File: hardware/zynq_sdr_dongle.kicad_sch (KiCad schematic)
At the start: 13 parts, among them J10 Conn_01x13_Male, J11 Conn_01x16_Male

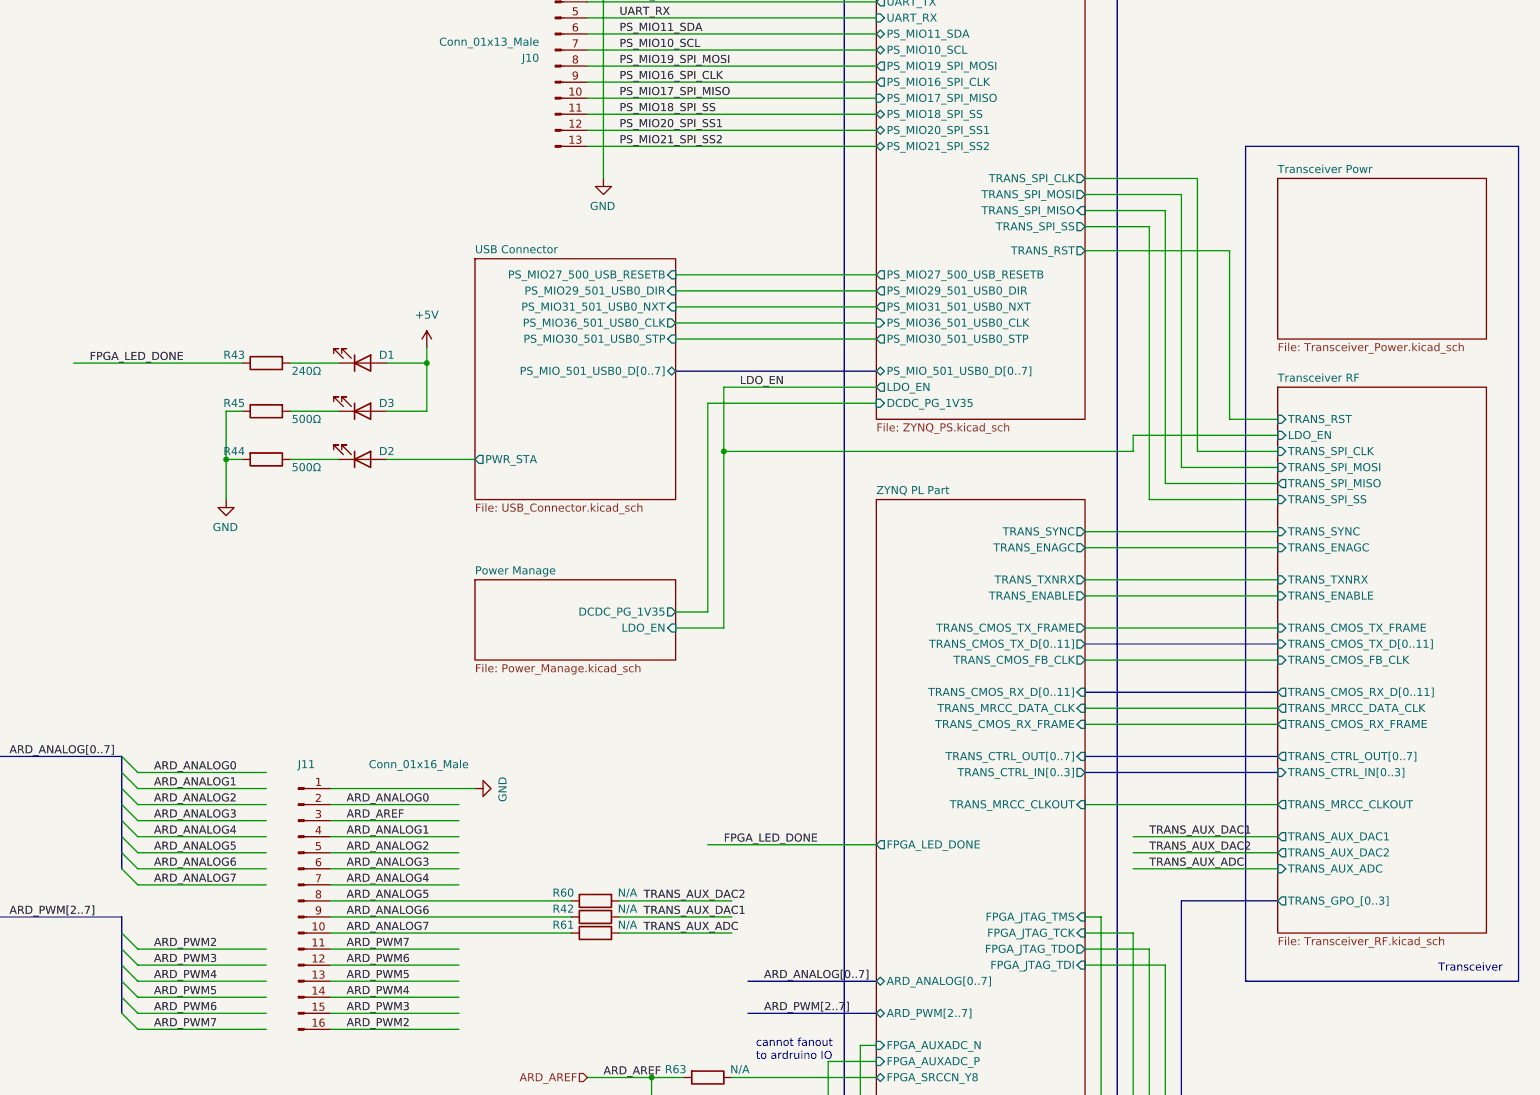
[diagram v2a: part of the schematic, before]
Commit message: Add PS I2C pullup resistor
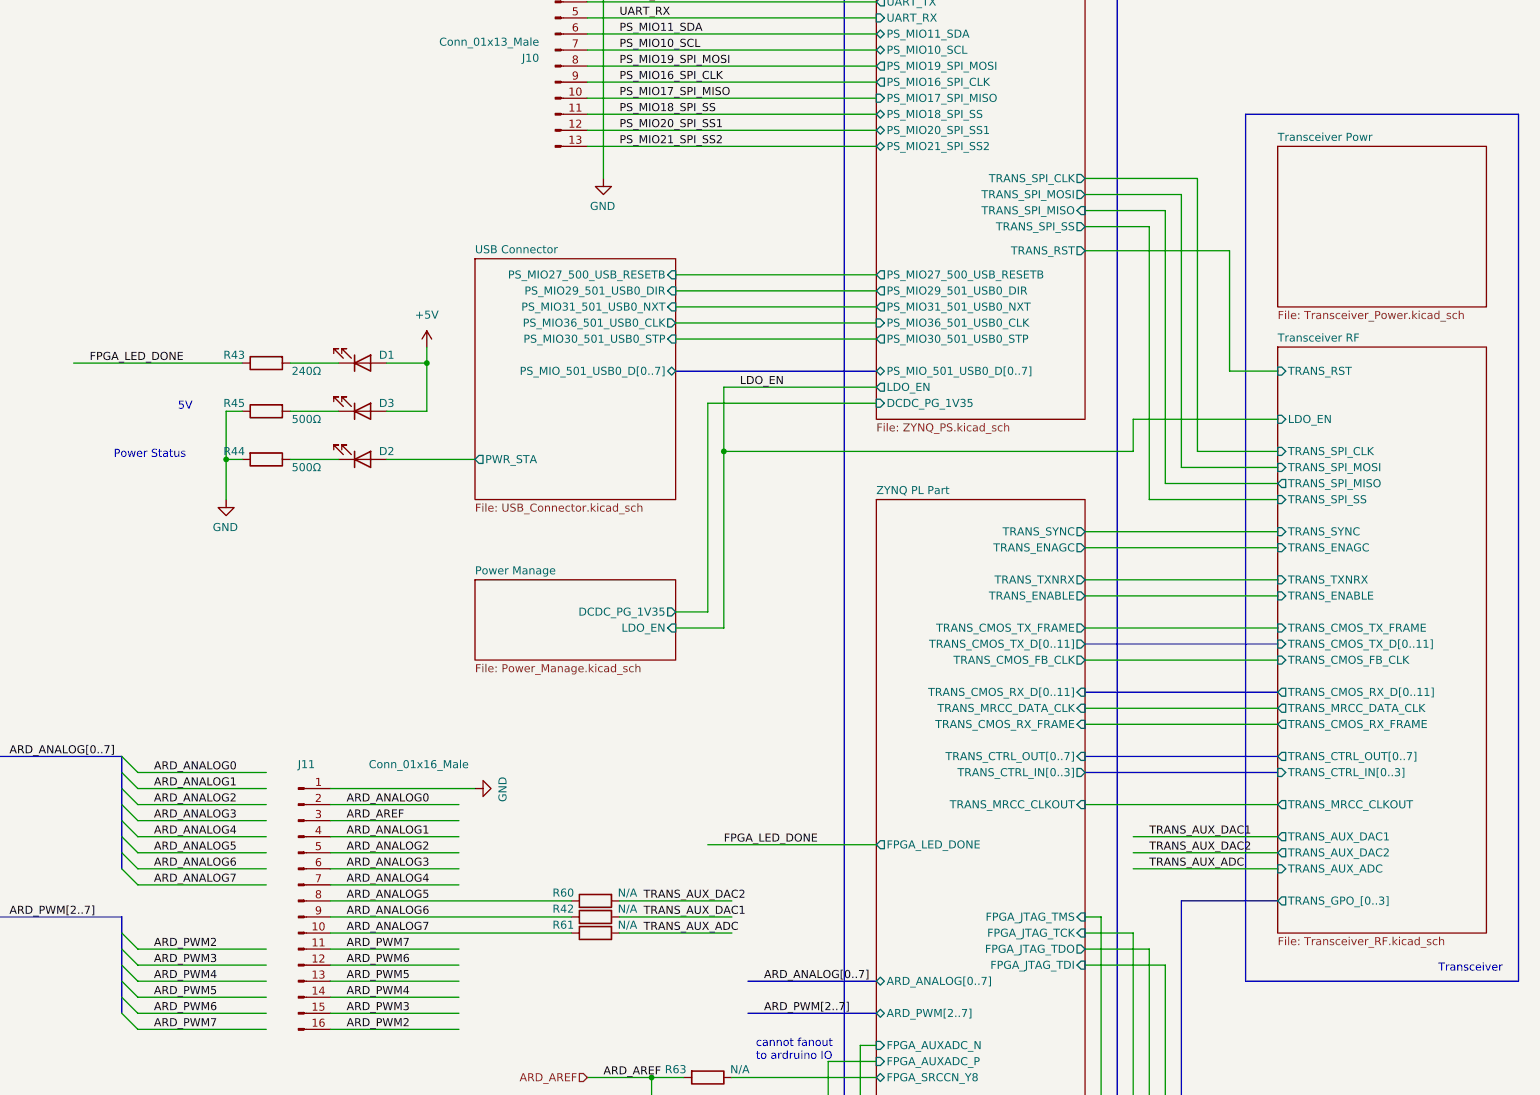
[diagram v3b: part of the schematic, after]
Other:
- note added: "5V"
- note added: "Power Status"
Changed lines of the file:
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@@
     (stroke (width 0) (type default))
   )
-  (wire (pts (xy 259.08 101.6) (xy 251.46 101.6))
+  (wire (pts (xy 259.08 93.98) (xy 251.46 93.98))
     (stroke (width 0) (type default))
   )
@@
     (stroke (width 0) (type default))
   )
-  (wire (pts (xy 236.22 104.14) (xy 259.08 104.14))
+  (wire (pts (xy 236.22 101.6) (xy 259.08 101.6))
     (stroke (width 0) (type default))
   )
@@
     (stroke (width 0) (type default))
   )
-  (wire (pts (xy 251.46 101.6) (xy 251.46 74.93))
+  (wire (pts (xy 251.46 93.98) (xy 251.46 74.93))
     (stroke (width 0) (type default))
   )
@@
     (stroke (width 0) (type default))
   )
-  (wire (pts (xy 236.22 106.68) (xy 236.22 104.14))
+  (wire (pts (xy 236.22 106.68) (xy 236.22 101.6))
     (stroke (width 0) (type default))
   )
@@
     (stroke (width 0) (type default))
   )
-  (rectangle (start 254 58.42) (end 297.18 190.5)
+  (rectangle (start 254 53.34) (end 297.18 190.5)
     (stroke (width 0.1524) (type default))
     (fill (type none))
@@
     (fill (type none))
   )
+  (text "5V" (at 85.09 100.33 0)
+    (effects (font (size 1.27 1.27)) (justify left bottom))
+  )
   (text "Transceiver" (at 284.48 189.23 0)
     (effects (font (size 1.27 1.27)) (justify left bottom))
@@
   )
   (text "cannot fanout\nto ardruino IO\n" (at 176.53 203.2 0)
+    (effects (font (size 1.27 1.27)) (justify left bottom))
+  )
+  (text "Power Status\n" (at 74.93 107.95 0)
     (effects (font (size 1.27 1.27)) (justify left bottom))
   )
@@
     )
   )
-  (sheet (at 259.08 96.52) (size 33.02 86.36) (fields_autoplaced)
+  (sheet (at 259.08 90.17) (size 33.02 92.71) (fields_autoplaced)
     (stroke (width 0.1524) (type solid))
     (fill (color 0 0 0 0.0000))
-    (property "Sheetname" "Transceiver RF" (id 0) (at 259.08 95.8084 0)
+    (property "Sheetname" "Transceiver RF" (id 0) (at 259.08 89.4584 0)
       (effects (font (size 1.27 1.27)) (justify left bottom))
     )
@@
       (effects (font (size 1.27 1.27)) (justify left))
     )
-    (pin "TRANS_RST" input (at 259.08 101.6 180)
-      (effects (font (size 1.27 1.27)) (justify left))
-    )
-    (pin "LDO_EN" input (at 259.08 104.14 180)
-      (effects (font (size 1.27 1.27)) (justify left))
-    )
-  )
-  (sheet (at 259.08 63.5) (size 33.02 25.4) (fields_autoplaced)
+    (pin "TRANS_RST" input (at 259.08 93.98 180)
+      (effects (font (size 1.27 1.27)) (justify left))
+    )
+    (pin "LDO_EN" input (at 259.08 101.6 180)
+      (effects (font (size 1.27 1.27)) (justify left))
+    )
+  )
+  (sheet (at 259.08 58.42) (size 33.02 25.4) (fields_autoplaced)
     (stroke (width 0.1524) (type solid))
     (fill (color 0 0 0 0.0000))
-    (property "Sheetname" "Transceiver Powr" (id 0) (at 259.08 62.7884 0)
+    (property "Sheetname" "Transceiver Powr" (id 0) (at 259.08 57.7084 0)
       (effects (font (size 1.27 1.27)) (justify left bottom))
     )
-    (property "Sheetfile" "Transceiver_Power.kicad_sch" (id 1) (at 259.08 89.4846 0)
+    (property "Sheetfile" "Transceiver_Power.kicad_sch" (id 1) (at 259.08 84.4046 0)
       (effects (font (size 1.27 1.27)) (justify left top))
     )
@@
       (reference "#PWR0237") (unit 1) (value "GND") (footprint "")
     )
-    (path "/2e492126-6191-42ba-8e02-c3a9e141c50a/6311da68-6122-4903-be68-cdff269f6d29"
-      (reference "#PWR0238") (unit 1) (value "GND") (footprint "")
-    )
-    (path "/2e492126-6191-42ba-8e02-c3a9e141c50a/a6f39143-8618-4dc1-9481-e0a08978eabf"
-      (reference "#PWR0239") (unit 1) (value "+1V8") (footprint "")
+    (path "/2e492126-6191-42ba-8e02-c3a9e141c50a/5f5e850e-342f-41c6-81d1-bb27c4f59d7c"
+      (reference "#PWR0238") (unit 1) (value "+1V8") (footprint "")
+    )
+    (path "/2e492126-6191-42ba-8e02-c3a9e141c50a/45708189-6cf6-4828-a1a1-fe879b822edb"
+      (reference "#PWR0239") (unit 1) (value "GND") (footprint "")
     )
     (path "/639f24e7-f472-4c97-971a-e363c3f9fd3c/19b194a1-aaa8-4204-9d7a-386064fa933a"
@@
       (reference "#PWR0260") (unit 1) (value "+1V8") (footprint "")
     )
+    (path "/2e492126-6191-42ba-8e02-c3a9e141c50a/a756a93b-d67c-4865-ac49-bf164ddfaadd"
+      (reference "#PWR0261") (unit 1) (value "GND") (footprint "")
+    )
     (path "/f2fd7566-1c55-48f1-b9cf-73bb6d17f3a6/87d5bad7-9677-46e4-90d9-9d7b66b6831a/310d2724-6c6d-4c1a-b72d-1691fc5ddc1c"
       (reference "#PWR0263") (unit 1) (value "+1V8") (footprint "")
@@
     )
     (path "/2e492126-6191-42ba-8e02-c3a9e141c50a/553b6258-7c38-4e45-b121-526cccdfe90b"
-      (reference "C80") (unit 1) (value "0.1uF") (footprint "Capacitor_SMD:C_0201_0603Metric")
+      (reference "C80") (unit 1) (value "18pF") (footprint "Capacitor_SMD:C_0201_0603Metric")
     )
     (path "/2e492126-6191-42ba-8e02-c3a9e141c50a/6bf1253c-6fc3-41c7-a0af-e49db97f2dde"
-      (reference "C81") (unit 1) (value "0.1uF") (footprint "Capacitor_SMD:C_0201_0603Metric")
+      (reference "C81") (unit 1) (value "18pF") (footprint "Capacitor_SMD:C_0201_0603Metric")
     )
     (path "/639f24e7-f472-4c97-971a-e363c3f9fd3c/0c4ebf32-1ee5-47da-9663-10130c1af94b"
@@
       (reference "J13") (unit 1) (value "Conn_01x04_Male") (footprint "Connector_Local:BM03B-ACHSS-GAN-TF")
     )
+    (path "/2e492126-6191-42ba-8e02-c3a9e141c50a/5595eeb4-f057-40f7-9141-b39aabd80bc8"
+      (reference "J14") (unit 1) (value "Conn_01x01") (footprint "Connector_PinHeader_2.54mm:PinHeader_1x01_P2.54mm_Vertical")
+    )
     (path "/048e1ae9-e0b6-40ad-ad10-0b910f122731/c3571cb6-3ddd-4074-ae5a-0b38e284b57b"
       (reference "L1") (unit 1) (value "DFE18SANR47MG0") (footprint "Inductor_SMD:L_Murata_LQH2MCNxxxx02_2.0x1.6mm")
@@
       (reference "R66") (unit 1) (value "10K") (footprint "Resistor_SMD:R_0201_0603Metric")
     )
+    (path "/2e492126-6191-42ba-8e02-c3a9e141c50a/84159df1-2a43-4894-9f71-67dad2a59905"
+      (reference "R67") (unit 1) (value "0R") (footprint "Resistor_SMD:R_0201_0603Metric")
+    )
+    (path "/2e492126-6191-42ba-8e02-c3a9e141c50a/727fbeee-a3d1-4c3d-82c0-90bdfeae389e"
+      (reference "R68") (unit 1) (value "N/A") (footprint "Resistor_SMD:R_0201_0603Metric")
+    )
     (path "/f2fd7566-1c55-48f1-b9cf-73bb6d17f3a6/87d5bad7-9677-46e4-90d9-9d7b66b6831a/18a63771-9e2a-4028-b4a2-e050470b986b"
       (reference "SW2") (unit 1) (value "SW_DIP_x01") (footprint "Switcher:EVQ9P701P")
@@
       (reference "U11") (unit 1) (value "TPS2121") (footprint "Capacitor_SMD_Local:VQFN-12_2p0_2p5_0p5")
     )
-    (path "/2e492126-6191-42ba-8e02-c3a9e141c50a/05d6223a-0f74-4fb5-b20d-72b54a079563"
-      (reference "U12") (unit 1) (value "Si513A_2.5x3.2mm") (footprint "Oscillator:Oscillator_SMD_Silicon_Labs_LGA-6_2.5x3.2mm_P1.25mm")
-    )
     (path "/f2fd7566-1c55-48f1-b9cf-73bb6d17f3a6/87d5bad7-9677-46e4-90d9-9d7b66b6831a/5886c2df-6286-440b-8e47-50ca1422d30b"
       (reference "U13") (unit 1) (value "TXS0206A") (footprint "Package_CSP_Local:WLCSP-20_1.609x1.994mm_Layout4x5_P0.4mm")
@@
     )
     (path "/f2fd7566-1c55-48f1-b9cf-73bb6d17f3a6/87d5bad7-9677-46e4-90d9-9d7b66b6831a/eae31dc2-663f-4ce4-9f3f-5fe5974a5281"
-      (reference "X2") (unit 1) (value "ECS-2520MV-xxx-xx") (footprint "Oscillator:Oscillator_SMD_ECS_2520MV-xxx-xx-4Pin_2.5x2.0mm")
-    )
-  )
+      (reference "X2") (unit 1) (value "SiT1602B") (footprint "Oscillator:Oscillator_SMD_ECS_2520MV-xxx-xx-4Pin_2.5x2.0mm")
+    )
+    (path "/2e492126-6191-42ba-8e02-c3a9e141c50a/3bb8fbe4-dbc8-4f72-9892-82c13f0e0c73"
+      (reference "X3") (unit 1) (value "SiT1602B") (footprint "Oscillator:Oscillator_SMD_ECS_2520MV-xxx-xx-4Pin_2.5x2.0mm")
+    )
+  )

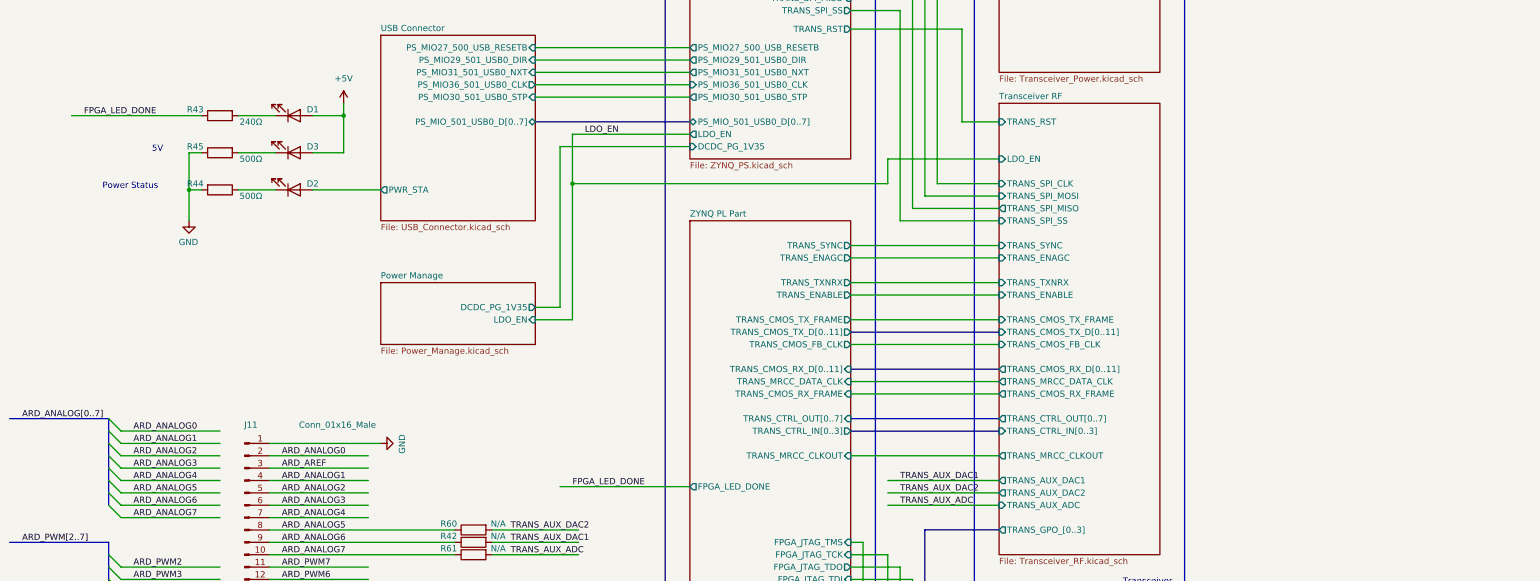
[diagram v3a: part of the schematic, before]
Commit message: Modify wrong DCDC TPS62088 package Panelize PCB Add manufacture requirements files
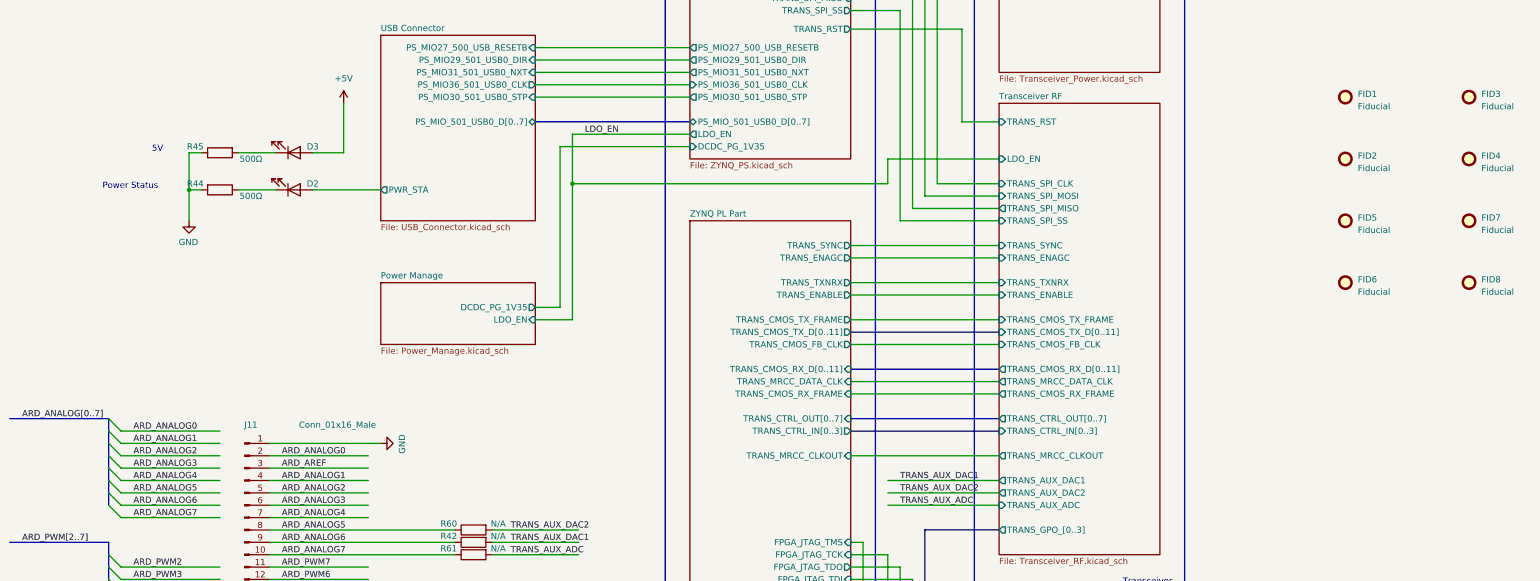
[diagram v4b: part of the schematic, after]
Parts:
- removed D1: LED, LED_SMD:LED_0201_0603Metric, symbol Device:LED
- removed R43: 240Ω, Resistor_SMD:R_0201_0603Metric, symbol Device:R
- added FID1, FID2, FID3, FID4, FID5, FID6, FID7, FID8: Fiducial, Fiducial:Fiducial_0.75mm_Mask2.25mm, symbol Mechanical:Fiducial
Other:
- sheet ZYNQ PL Part ports: added none; removed FPGA_LED_DONE
